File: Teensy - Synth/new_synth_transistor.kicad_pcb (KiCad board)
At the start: 6 copper layers, 58 parts, among them J1 Conn_01x07_Female, Q1 MMBT3904, Q2 MMBT3904, Q3 eMMBT3904, Q4 MMBT3904, U1 LM324, U10 LM555, U11 SN74HC02NSR, U12 LM324, U2 LM324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

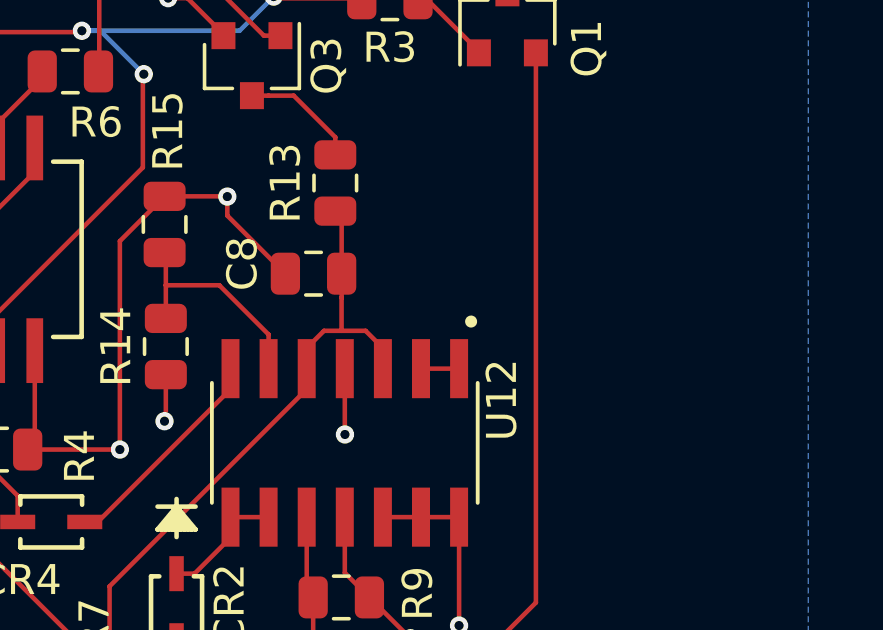
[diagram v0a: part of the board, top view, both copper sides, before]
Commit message: Add ADSR Singal
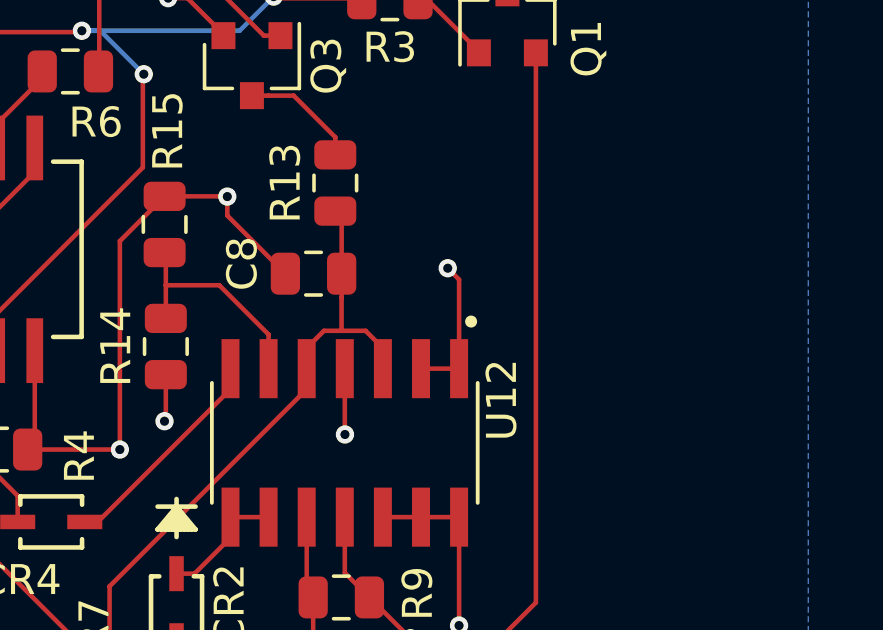
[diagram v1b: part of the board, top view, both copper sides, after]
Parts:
- Q3: value eMMBT3904 -> MMBT3904
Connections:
- U8 pad 41: Net-(U8-Pad41) -> /ADSR_OUT
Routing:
- net /ADSR_OUT: track 1.27 -> 77.7 mm, vias 0 -> 1

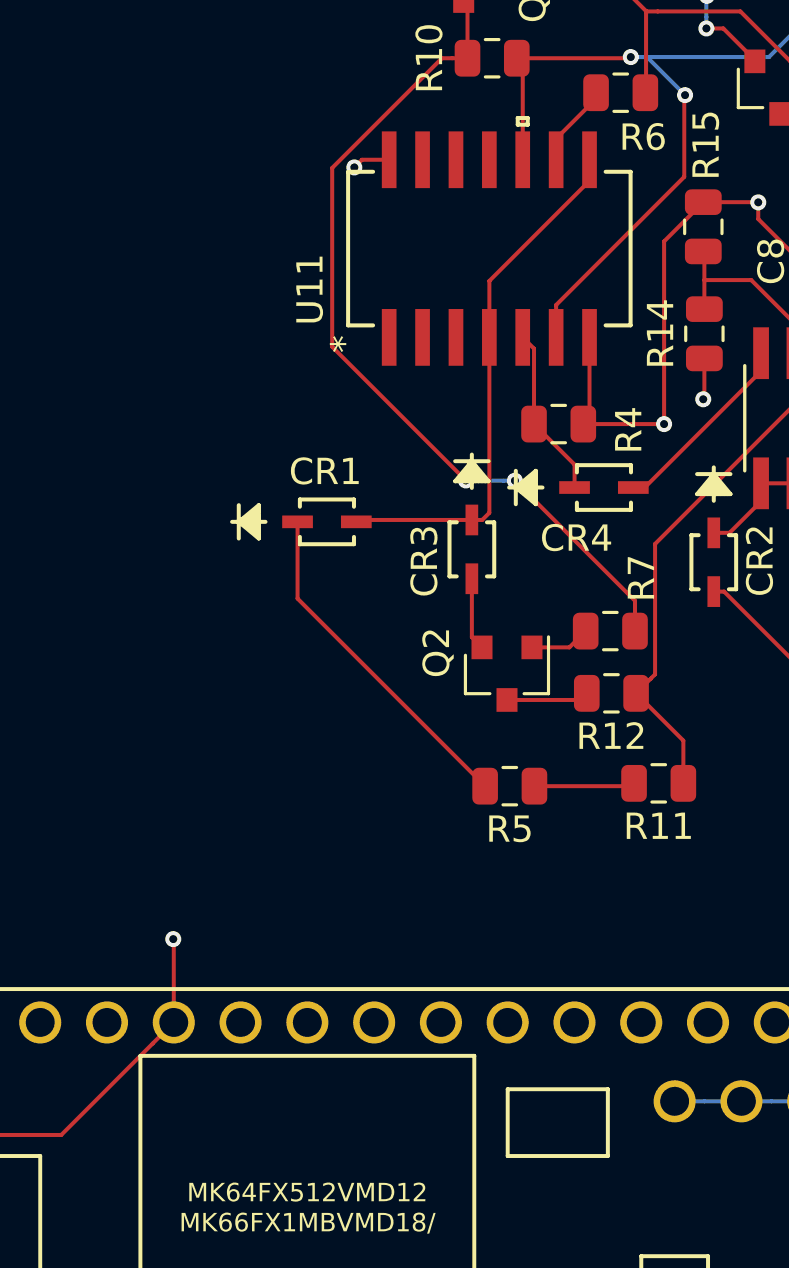
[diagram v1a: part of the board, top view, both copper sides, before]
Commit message: Add ADSR Signal
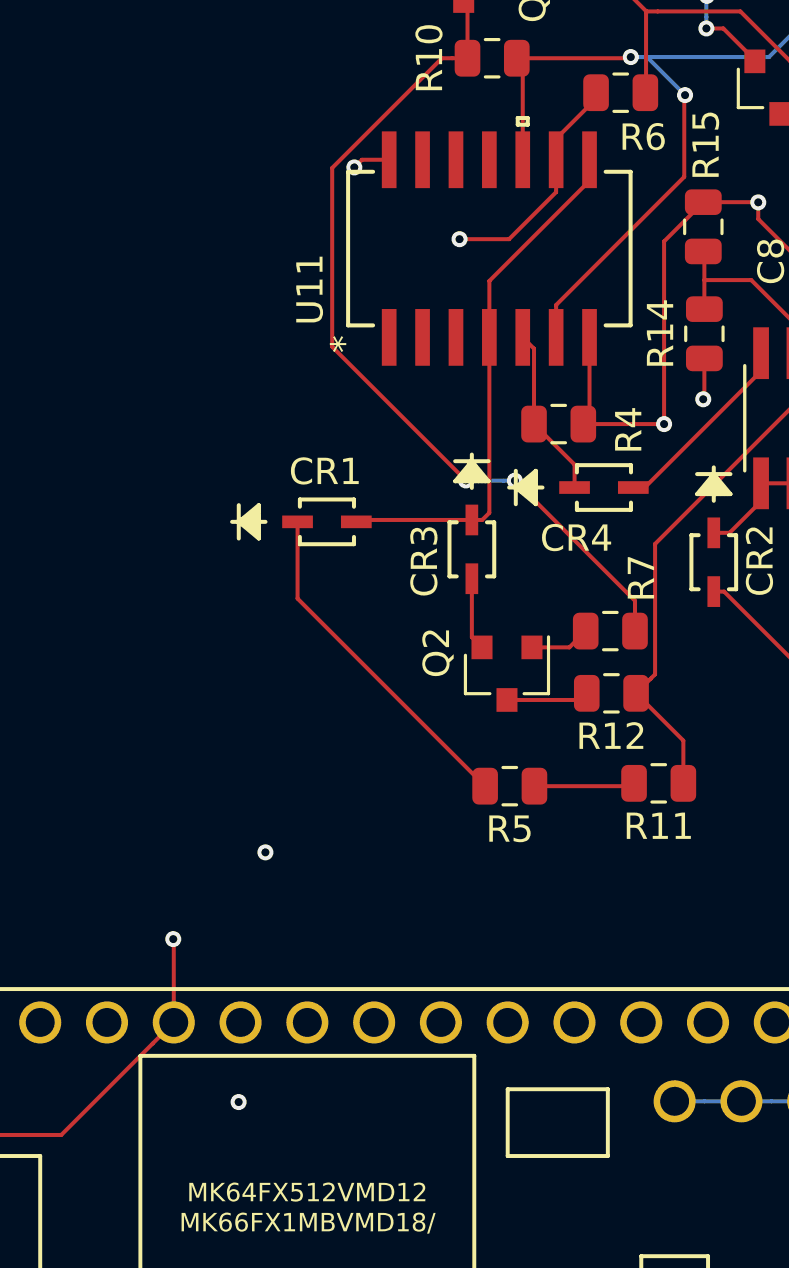
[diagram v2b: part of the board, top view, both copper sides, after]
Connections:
- U8 pad 37: Net-(U8-Pad37) -> /SIGNAL
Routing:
- net /SIGNAL: track 3.18 -> 63.5 mm, vias 0 -> 1
- net /ADSR_OUT: track 77.7 -> 59.0 mm
- net GNDREF: track 32.4 -> 42.6 mm, vias 5 -> 7

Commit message: dxf added to teensy pcb rev 2
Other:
- board outline added: 72.1 x 109.8 mm
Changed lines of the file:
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@@
-(kicad_pcb (version 20171130) (host pcbnew "(5.0.1)-4")
+(kicad_pcb (version 20171130) (host pcbnew 5.0.1-33cea8e~68~ubuntu18.04.1)
   (general
     (thickness 1.6)
-    (drawings 0)
+    (drawings 8)
     (tracks 505)
     (zones 0)
@@
     (0 F.Cu signal)
     (1 VCC signal hide)
-    (2 GNDREF signal)
+    (2 GNDREF signal hide)
     (3 3.3 signal hide)
     (4 In4.Cu signal)
@@
   )
   (setup
-    (last_trace_width 0.3048)
+    (last_trace_width 0.1524)
     (user_trace_width 0.1524)
     (user_trace_width 0.3048)
@@
       (net 97 "Net-(C6-Pad2)"))
   )
+  (gr_arc (start 282.859783 123.225341) (end 282.858578 124.469901) (angle -88.87597927) (layer Edge.Cuts) (width 0.2))
+  (gr_arc (start 213.422165 123.29672) (end 212.19668 123.32716) (angle -89.70790033) (layer Edge.Cuts) (width 0.2))
+  (gr_arc (start 213.435827 16.048209) (end 213.45652 14.76248) (angle -90.90025952) (layer Edge.Cuts) (width 0.2))
+  (gr_arc (start 282.915359 16.052799) (end 284.2006 16.09344) (angle -92.7) (layer Edge.Cuts) (width 0.2))
+  (gr_line (start 212.15096 16.01216) (end 212.20176 123.42876) (layer Edge.Cuts) (width 0.2))
+  (gr_line (start 282.92552 124.47524) (end 213.34476 124.53112) (layer Edge.Cuts) (width 0.2))
+  (gr_line (start 284.2006 16.02232) (end 284.13456 123.25096) (layer Edge.Cuts) (width 0.2))
+  (gr_line (start 213.3854 14.76248) (end 282.88996 14.76248) (layer Edge.Cuts) (width 0.2))
   (segment (start 269.651529 39.753212) (end 270.921529 39.753212) (width 0.1524) (layer F.Cu) (net 0))
   (segment (start 272.191529 39.753212) (end 270.921529 39.753212) (width 0.1524) (layer F.Cu) (net 0))
@@
   (segment (start 254.988402 30.4673) (end 253.10338 30.4673) (width 0.1524) (layer F.Cu) (net 19))
   (via (at 253.10338 30.4673) (size 0.6096) (drill 0.3048) (layers F.Cu GND) (net 19))
-  (segment (start 252.798581 30.772099) (end 253.10338 30.4673) (width 0.3048) (layer GNDREF) (net 19))
-  (segment (start 233.462319 50.108361) (end 252.798581 30.772099) (width 0.3048) (layer GNDREF) (net 19))
   (segment (start 233.462319 71.806559) (end 233.462319 50.108361) (width 0.3048) (layer GNDREF) (net 19))
   (segment (start 237.15472 75.49896) (end 233.462319 71.806559) (width 0.3048) (layer GNDREF) (net 19))
+  (segment (start 233.462319 50.108361) (end 252.798581 30.772099) (width 0.3048) (layer GNDREF) (net 19))
+  (segment (start 252.798581 30.772099) (end 253.10338 30.4673) (width 0.3048) (layer GNDREF) (net 19))
   (segment (start 272.191529 34.803212) (end 270.921529 34.803212) (width 0.1524) (layer F.Cu) (net 20))
   (segment (start 272.191529 34.803212) (end 272.191529 31.833869) (width 0.1524) (layer F.Cu) (net 20))
@@
     (polygon
       (pts
-        (xy 212.83676 15.66164) (xy 212.83676 132.88772) (xy 283.80944 133.81736) (xy 283.83484 15.75816)
+        (xy 194.95008 17.51076) (xy 194.06108 134.01548) (xy 299.847 134.6708) (xy 298.03344 15.91564)
       )
     )
@@
     (polygon
       (pts
-        (xy 212.59292 14.4272) (xy 285.20136 15.24) (xy 285.63824 138.7348) (xy 206.93888 136.54024)
+        (xy 188.087 15.62608) (xy 296.56024 13.73124) (xy 300.5836 138.30808) (xy 192.65392 137.88136)
       )
     )
@@
     (polygon
       (pts
-        (xy 209.81924 13.68552) (xy 285.91764 14.29512) (xy 290.21024 147.96008) (xy 202.93076 142.38732)
+        (xy 185.33872 13.80744) (xy 309.3974 13.6652) (xy 314.96508 146.49704) (xy 177.8508 143.49984)
       )
     )
@@
     (polygon
       (pts
-        (xy 208.02092 12.5222) (xy 286.75584 12.82192) (xy 289.74796 150.53564) (xy 201.73188 145.4404)
+        (xy 170.80992 15.65148) (xy 311.01792 13.79728) (xy 310.08828 152.146) (xy 187.52312 144.71904)
       )
     )

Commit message: 2 layers
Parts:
- moved R1 22.2 mm to (243.0, 49.1), turned to 90 degrees
- moved R2 19.4 mm to (243.0, 45.3), turned to 90 degrees
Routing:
- net +5V: track 98.5 -> 355.9 mm, vias 18 -> 16
- net GNDREF: track 42.6 -> 91.4 mm, vias 7 -> 3
- net +3V3: track 22.3 -> 62.7 mm, vias 3 -> 1
- net /ADSR_OUT: track 59.0 -> 75.9 mm, vias 1 -> 2
- net /SIGNAL: track 63.5 -> 61.0 mm
- net Net-(Q4-Pad3): track 32.6 -> 34.6 mm
- removed copper zone on 3.3, net +3V3
- removed copper zone on VCC, net +5V
- removed copper zone on GNDREF, net GNDREF
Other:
- copper layers 6 -> 2
